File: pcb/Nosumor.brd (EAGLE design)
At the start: 50 x 50 mm, 122 parts, among them IC1 STM32F722RET, J3 SJ-43515TS-SMT-EDGE, K1 CHERRY-MX, K2 CHERRY-MX, K3 KSC623J, K4 KSC623J, K5 KSC623J, Q1 FDY100PZ, Q2 FDY100PZ, Q3 FDY100PZ, Q4 FDY100PZ, Q5 ABMM-6.000MHZ, Q6 CX2016DB, U2 AP2112K-3.3V, U3 USB3370, U4 TLV320AIC3110, U5 AP2112K-1.8V, U6 9DoF IMU

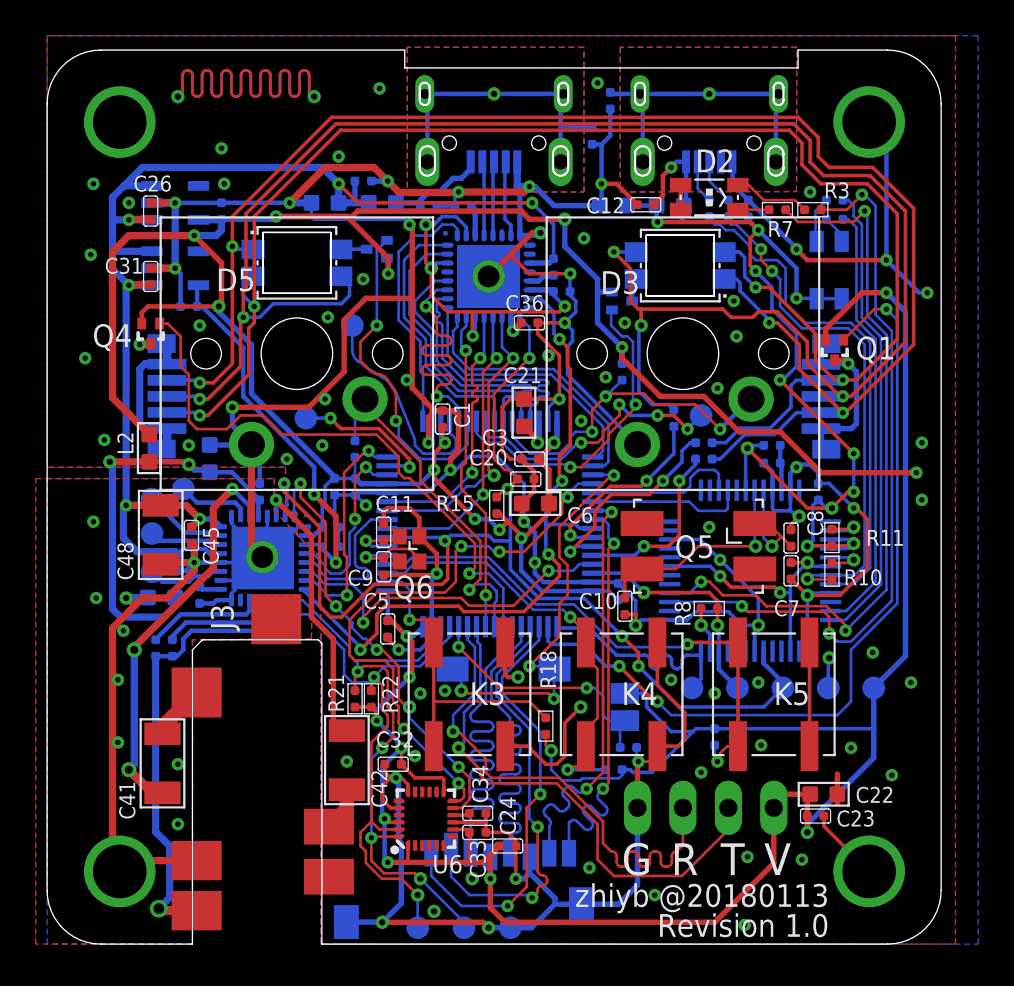
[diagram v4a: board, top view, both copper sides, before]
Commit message: PCB version 1.1 connected
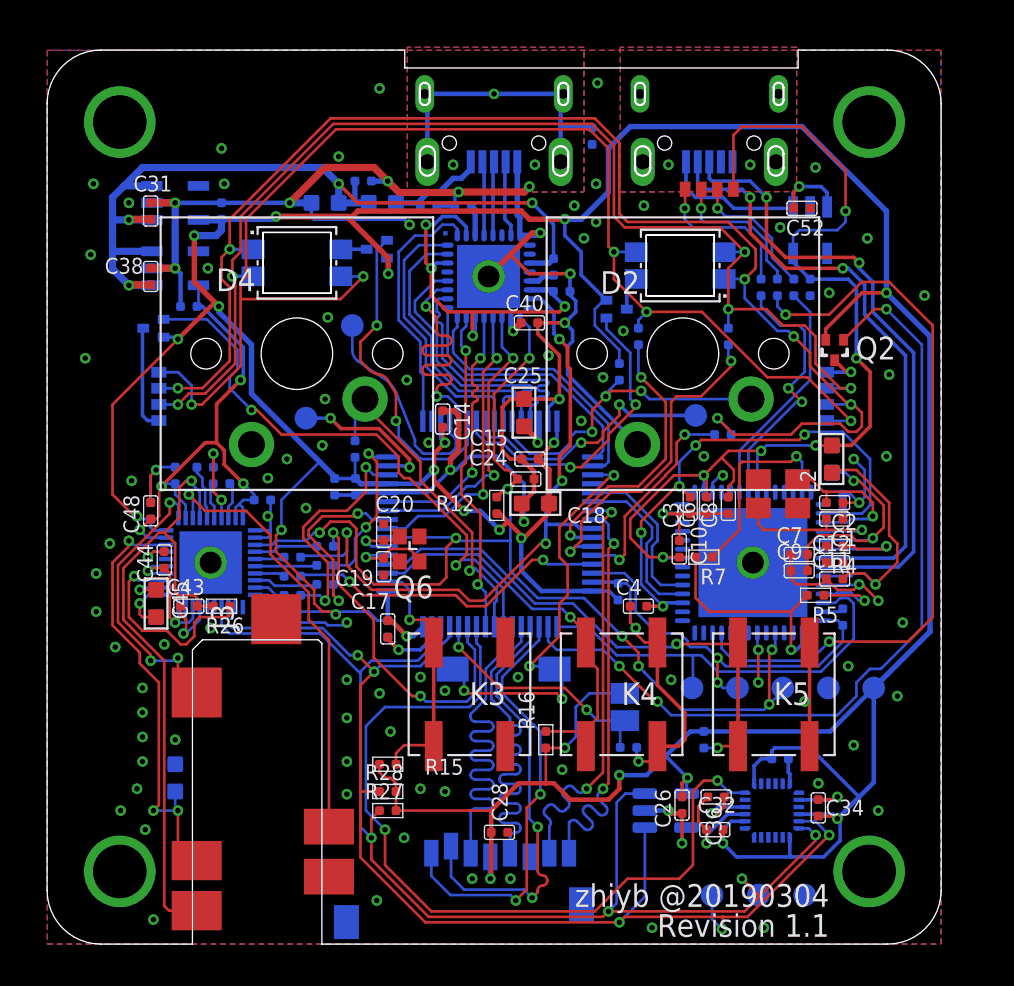
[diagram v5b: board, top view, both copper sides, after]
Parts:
- removed A2, GND$2, SCL, SDA, SLM, SLP, SRM, SRP: TPB1,27, testpad:B1,27
- removed D6: MSL0104RGBU1, led:2709
- removed JP1: (no value), pinhead:1X04
- added C50, C51: 100nf, Seeed-Capacitor:C0402
- added C52: 1UF 6.3V, Seeed-Capacitor:C0402
- added L4: 120OHM-500MA, Seeed-Inductor:L0603
- added R26: 2k7, Seeed-Resistor:R0402
- added R27, R28: 2k2, Seeed-Resistor:R0402
- added TP1, TP2, TP3, TP7: TPB1,27, testpad:B1,27
- added U7: AP2112K-1.8V, SparkFun-IC-Power:SOT23-5
- added U8: 24CW1280T-I/OT, 24CW1280T-I_OT:SOT95P280X145-5N
- C1, C2: value 100nf -> 4p
- C10, C8: value 18pf -> 100nf
- C11: value 12pf -> 4u7
- C13, C37, C39: value 100nf -> 1UF 6.3V
- C14, C33: value 10nf -> 100nf
- C17, C30, C35: value 1UF 6.3V -> 100nf
- C18: value 10uf -> 4.7uf
- C19, C20: value 100nf -> 12pf
- C21: value 4.7uf -> 10nf; device Seeed-Capacitor:C0603 -> Seeed-Capacitor:C0402
- C22: value 10uf -> 1UF 6.3V; device Seeed-Capacitor:C0603 -> Seeed-Capacitor:C0402
- C25: value 100nf -> 4.7uf; device Seeed-Capacitor:C0402 -> Seeed-Capacitor:C0603
- C26, C36: value 1UF 6.3V -> 100n
- C27, C32, C34: value 100nf -> 100n
- C28, C43, C44: value 10uf -> 100nf; device Seeed-Capacitor:C0603 -> Seeed-Capacitor:C0402
- C29, C46: value 100nf -> 2u2
- C4: value 100nf -> 3u3
- C40: value 470nf -> 1UF 6.3V
- C41: value 100uf -> 1UF 6.3V; device Seeed-Capacitor:C1206 -> Seeed-Capacitor:C0402
- C42, C48: value 100uf -> 100nf; device Seeed-Capacitor:C1206 -> Seeed-Capacitor:C0402
- C45, C47: value 100nf -> 10uf; device Seeed-Capacitor:C0402 -> Seeed-Capacitor:C0603
- C6: value 4.7uf -> 100nf; device Seeed-Capacitor:C0603 -> Seeed-Capacitor:C0402
- C7: value 33nf -> 4u7
- C9: value 12pf -> 100nf
- D1: value APBD3224SURKCGKC-F01 -> MSL0601RGB; device led:1210 -> led:1105
- D2: value APBD3224SURKCGKC-F01 -> HSMF-A3-BACK; device led:1210 -> led:HSMF-A3-BACK
- D3, D5: value HSMF-A3-BACK -> MSL0601RGB; device led:HSMF-A3-BACK -> led:1105
- D4: value MSL0104RGBU1 -> HSMF-A3-BACK; device led:2709 -> led:HSMF-A3-BACK
- Q1: value FDY100PZ -> ABM8W-12.0000MHZ; device transistor:SC-89 -> crystal:ABM8W
- Q5: value ABMM-6.000MHZ -> FDY100PZ; device crystal:ABMM -> transistor:SC-89
- R10: value 1.5K -> 150R
- R12, R13: value 22R -> 10K 1/16W
- R18, R19, R20: value 10K 1/16W -> 27R
- R2: value 150R -> 330R
- R21, R22: value 2.2K -> 27R
- R23: value 10K 1/16W -> 10R
- R24: value 20K -> 10K 1/16W
- R25: value 2.2K -> 20K
- R4: value 150R -> 12K 1/16W
- R5: value 330R -> 2k2
- R6: value 150R -> 470R 1/16W
- R7: value 330R -> 10K 1/16W
- R8, R9: value 470R 1/16W -> 150R
- U1: value (none) -> FT2232H-56Q-REEL; device ftdichip-6:LQFP48 -> FT2232H-56Q-REEL:QFN50P800X800X100-57N
- U3: value USB3370 -> AP2112K-3.3V; device microchip:QFN32 -> SparkFun-IC-Power:SOT23-5
- U4: value TLV320AIC3110 -> USB3370; device ti:VQFN32 -> microchip:QFN32
- U5: value AP2112K-1.8V -> TLV320AIC3256; device SparkFun-IC-Power:SOT23-5 -> ti:QFN40P500X500X80-41N
- moved C26 44.6 mm to (35.5, 7.77), turned to 180 degrees
- moved L2 38.2 mm to (43.9, 27.1)
- moved U2 35.5 mm to (42.7, 39.9), turned to 180 degrees
- moved Q5 32.8 mm to (5.94, 34.4), flipped to the bottom, turned to 270 degrees
- moved C42 32.4 mm to (17.7, 42.7), flipped to the bottom, turned to 90 degrees
- moved C22 32.3 mm to (16.1, 25.6), flipped to the bottom, turned to 180 degrees
- moved D4 30.2 mm to (14.0, 38.1), flipped to the top, turned to 270 degrees
- moved R25 30.1 mm to (28.3, 37.9), turned to 180 degrees
- moved C49 30.1 mm to (7.16, 26.2)
- moved C36 28.5 mm to (37.4, 8.23), turned to 90 degrees
- moved C27 27.8 mm to (41.0, 10.4)
- moved C40 27.7 mm to (27.0, 34.7), flipped to the top, turned to 270 degrees
- moved C5 26.4 mm to (44.5, 24.7), flipped to the bottom, turned to 0 degrees
- moved C23 26.1 mm to (19.1, 17.6), flipped to the bottom, turned to 180 degrees
- moved C41 25.6 mm to (7.92, 35.7), flipped to the bottom, turned to 270 degrees
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- renumbered A1 to TP4, BOOT to SJ1, CLK to TP6, D to TP8, DIO to TP9, GND to TP10, RST to TP5, VDD to TP11
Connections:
- removed net AVDD: C28.2, C29.2, C37.2, C43.2, L2.1, U4.17, U4.28
- removed net DBG_5V: C13.2, C16.2, C18.2, D1.1, D1.3, D2.1, D2.3, L1.1, R11.2, R9.2, U1.3, U1.4, U1.42
- removed net DBG_BM_U: J1.2, R12.2
- removed net DBG_DM: R12.1, U1.8
- removed net DBG_DP: R10.2, R13.1, U1.7
- removed net DBG_DP_U: J1.3, R13.2
- removed net DBG_SWD_LED1: R5.1, U1.12
- removed net DBG_SWD_LED2: R1.1, U1.11
- removed net N$10: C7.1, U1.14, U1.31, U1.6
- removed net N$27: C15.2, J1.Z1, J1.Z2, J1.Z3, J1.Z4
- removed net N$44: SRP.TP, U4.26
- removed net N$45: SRM.TP, U4.23
- removed net N$46: C40.1, U4.14
- removed net N$48: C42.1, U4.30
- removed net N$49: R25.1, U4.12
- removed net N$50: C41.1, U4.27
- removed net UART_RX: IC1.59, JP1.3
- removed net UART_TX: IC1.58, JP1.2
- new net DBG_1V8: C3.2, C4.2, C5.2, U1.2, U1.31, U1.43
- new net DBG_3V3: C10.2, C13.2, C6.2, C8.2, D1.CA, L1.2, L2.2, R5.2, R7.2, U1.16, U1.36, U1.44, U1.50, U2.5
- new net DBG_SWD_LED: R3.1, U1.25
- new net N$15: R7.1, U1.55
- new net N$16: D1.R, R1.2
- new net N$22: R20.2, U5.6
- new net N$40: R23.2, U5.5
- new net N$41: D1.B, R3.2
- new net N$42: C52.2, J1.1, U2.1, U2.3
- new net N$43: J1.3, U1.8
- new net N$51: J1.2, U1.7
- new net N$52: R4.1, U1.6
- new net N$53: R5.1, U1.11
- new net N$54: C7.2, C9.2, L1.1, U1.5
- new net N$55: C11.2, C12.2, L2.1, U1.9
- new net N$56: R6.2, U1.13
- new net N$8: C2.2, Q1.P$3, U1.3
- new net N$9: C1.2, Q1.P$1, U1.4
- net +1V8: now also C33.2, C41.2, C48.1, C49.1, U5.29, U5.32, U5.39, U5.40, U7.5; no longer C27.2, C38.2, U4.3, U5.5
- net +3V3: now also C15.2, C16.2, C18.2, C21.2, C26.2, C27.2, C28.1, C34.2, C35.2, C37.2, Q5.3, R12.2, R13.2, R14.2, R27.2, R28.2, U3.5, U5.10, U5.30, U8.4; no longer C1.2, C19.2, C24.1, C25.2, C3.2, C33.2, C4.2, C5.2, C6.2, JP1.1, L2.2, Q1.3, R18.2, R19.2, R20.2, R21.2, R22.2, U2.5, U4.2
- net +5V: now also C38.2, C42.2, C47.2, R25.2, U3.1, U3.3, U4.11, U7.1, U7.3; no longer C26.2, C39.2, C44.2, C45.2, C46.2, C48.2, R24.2, U2.1, U2.3, U3.11, U4.21, U4.24, U5.1, U5.3
- net ADC2: now also TP7.TP; no longer A2.TP
- net AIC_BCLK: now also R20.1; no longer U4.7
- net AIC_DIN: now also R19.1; no longer U4.5
- net AIC_DOUT: now also R21.1; no longer U4.4
- net AIC_GPIO: now also IC1.59, R18.1; no longer U4.32, U6.11
- net AIC_WCLK: now also R22.1; no longer U4.6
- net BOOT0: now also R11.1; no longer R14.1
- net DBG_RXD: now also U1.33; no longer U1.39
- net DBG_RX_LED: now also R2.1, U1.48; no longer R7.1, U1.28
- net DBG_TXD: now also U1.32; no longer U1.40
- net DBG_TX_LED: now also R1.1, U1.49; no longer R3.1, U1.27
- net GND: now also C2.1, C24.1, C28.2, C40.1, C41.1, C42.1, C44.2, C45.2, C48.2, C49.2, C50.1, C51.1, C52.1, C7.1, J1.Z1, J1.Z2, J1.Z3, J1.Z4, L4.2, R11.2, R24.1, R4.2, TP3.TP, U1.10, U1.21, U1.41, U1.57, U3.2, U4.8, U5.1, U5.11, U5.16, U5.21, U5.37, U5.41, U7.2, U8.2; no longer C2.2, C24.2, C28.1, C43.1, C44.1, C45.1, C46.1, C48.1, C49.1, C7.2, GND$2.TP, J3.4, JP1.4, R14.2, R23.1, U1.18, U1.25, U1.34, U1.47, U1.9, U3.8, U3.EXP, U4.1, U4.16, U4.18, U4.20, U4.25, U4.29
- net I2C_SCL: now also R28.1, TP2.TP, U5.13, U8.1; no longer R21.1, SCL.TP, U4.10
- net I2C_SDA: now also R27.1, TP1.TP, U5.14, U8.3; no longer R22.1, SDA.TP, U4.9
- net KEY_1: now also R13.1; no longer R16.1
- net KEY_2: now also R14.1; no longer R17.1
- net KEY_3: now also R15.1; no longer R18.1
- net KEY_4: now also R16.1; no longer R19.1
- net KEY_5: now also R17.1; no longer R20.1
- net LED_1: now also Q4.1; no longer Q3.1
- net LED_2: now also Q3.1; no longer Q2.1
- net LED_3: now also Q2.1; no longer Q1.1
- net LED_4: now also Q5.1; no longer Q4.1
- net LED_B: now also R8.1; no longer R2.1
- net LED_G: now also R10.1; no longer R6.1
- net LED_R: now also R9.1; no longer R4.1
- net MCLK: now also R23.1, U4.15; no longer U3.15, U4.8
- net MPU_INT: now also IC1.58; no longer IC1.36
- net N$1: now also R22.2, U5.7; no longer C41.2, J3.2
- net N$11: now also D3.CA, Q2.2; no longer C2.1, R9.1, U1.46
- net N$12: now also J3.3, U5.33; no longer D1.4, R5.2
- net N$13: now also J3.2, U5.31; no longer C12.2, J1.1, L1.2
- net N$14: now also J3.4, L4.1, U5.28; no longer R10.1, U1.5
- net N$17: now also C43.2, J3.1, R26.2, U5.34; no longer R11.1, U1.2
- net N$18: now also R26.1, U5.23; no longer C8.2, Q5.1, U1.44
- net N$19: now also C43.1, U5.17; no longer C10.2, Q5.3, U1.43
- net N$2: now also R19.2, U5.8; no longer C42.2, J3.3
- net N$20: now also C44.1, U5.18, U5.19, U5.20, U5.24, U5.25; no longer D2.4, R7.2
- net N$21: now also C45.1, U5.22; no longer D2.2, R3.2
- net N$23: now also C46.1, U5.36; no longer D1.2, R1.2
- net N$24: now also C19.2; no longer C9.2
- net N$25: now also C46.2, U5.38; no longer R8.2, U1.23
- net N$26: now also C20.2; no longer C11.2
- net N$28: now also D5.CA, Q5.2; no longer D6.1, D6.2, D6.6, D6.7, Q4.2
- net N$29: now also C25.2; no longer C21.2
- net N$3: now also R21.2, U5.9; no longer C40.2, J3.1, R25.2, U4.11
- net N$30: now also D1.G, R2.2; no longer SLM.TP, U4.19
- net N$31: now also C50.2; no longer C47.2
- net N$32: now also R25.1, U4.13; no longer R24.1, U3.13
- net N$33: now also C39.2, U4.14, U4.2, U4.22, U4.30; no longer C35.2, U3.14, U3.2, U3.22, U3.30
- net N$34: now also D4.2, Q4.2; no longer D5.2, Q3.2
- net N$35: now also C51.2; no longer C49.2
- net N$36: now also C40.2, U4.18; no longer C36.2, U3.18
- net N$37: now also R24.2, U4.3; no longer R23.2, U3.3
- net N$38: now also C29.2, U5.35; no longer D4.1, D4.2, D4.6, D4.7, Q1.2
- net N$39: now also D2.2, Q3.2; no longer D3.2, Q2.2
- net N$4: now also U4.4; no longer U3.4
- net N$47: now also C36.2; no longer C34.2
- net N$5: now also U4.5; no longer U3.5
- net N$6: now also U4.7; no longer U3.7
- net N$7: now also R18.2, U5.4; no longer SLP.TP, U4.22
- net NRST_N: now also U1.20; no longer U1.16
- net RGB_B: now also D2.1, D3.B, D4.1, D5.B, R8.2; no longer D3.1, D4.3, D5.1, D6.3, R2.2
- net RGB_G: now also D2.4, D3.G, D4.4, D5.G, R10.2; no longer D3.4, D4.5, D5.4, D6.5, R6.2
- net RGB_R: now also D2.3, D3.R, D4.3, D5.R, R9.2; no longer D3.3, D4.4, D5.3, D6.4, R4.2
- net SRST_N: now also C24.2, R12.1, U1.19, U4.17, U5.3; no longer C20.2, R15.1, U1.17, U3.17, U4.31
- net SWCLK: now also U1.12; no longer U1.24
- net SWDIO: now also R6.1, U1.14; no longer R8.1, U1.22
- net ULPI_CLK: now also U4.27; no longer U3.27
- net ULPI_D0: now also U4.1; no longer U3.1
- net ULPI_D1: now also U4.32; no longer U3.32
- net ULPI_D2: now also U4.31; no longer U3.31
- net ULPI_D3: now also U4.28; no longer U3.28
- net ULPI_D4: now also U4.26; no longer U3.26
- net ULPI_D5: now also U4.25; no longer U3.25
- net ULPI_D6: now also U4.24; no longer U3.24
- net ULPI_D7: now also U4.23; no longer U3.23
- net ULPI_DIR: now also U4.19; no longer U3.19
- net ULPI_NXT: now also U4.21; no longer U3.21
- net ULPI_STP: now also U4.20; no longer U3.20
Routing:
- net GND: track 399.8 -> 197.7 mm, vias 103 -> 121
- net DBG_3V3: track 0.00 -> 73.1 mm, vias 0 -> 7
- net DBG_5V: track 57.1 -> 0.00 mm, vias 11 -> 0
- net N$22: track 47.7 -> 3.47 mm, vias 2 -> 0
- net DBG_SWD_LED: track 0.00 -> 41.5 mm, vias 0 -> 2
- net N$43: track 0.00 -> 35.4 mm, vias 0 -> 2
- net I2C_SCL: track 33.3 -> 68.1 mm, vias 2 -> 5
- net N$17: track 2.64 -> 37.2 mm
- net N$51: track 0.00 -> 34.5 mm, vias 0 -> 2
- net I2C_SDA: track 34.4 -> 68.3 mm
- net DBG_1V8: track 0.00 -> 31.0 mm, vias 0 -> 5
- net DBG_DP: track 29.3 -> 0.00 mm, vias 3 -> 0
- net UART_TX: track 29.1 -> 0.00 mm, vias 1 -> 0
- net UART_RX: track 28.8 -> 0.00 mm, vias 1 -> 0
- net DBG_DM: track 28.6 -> 0.00 mm
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- removed copper zone on layer 1, net N$27
- removed copper zone on layer 16, net N$27
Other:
- board text added: "Revision 1.1"
- board text added: "zhiyb @20190304"
- board text removed: "R"
- board text removed: "Revision 1.0"
- board text removed: "T"
- board text removed: "V"
- board text removed: "zhiyb @20180113"

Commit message: PCB with silkscreen
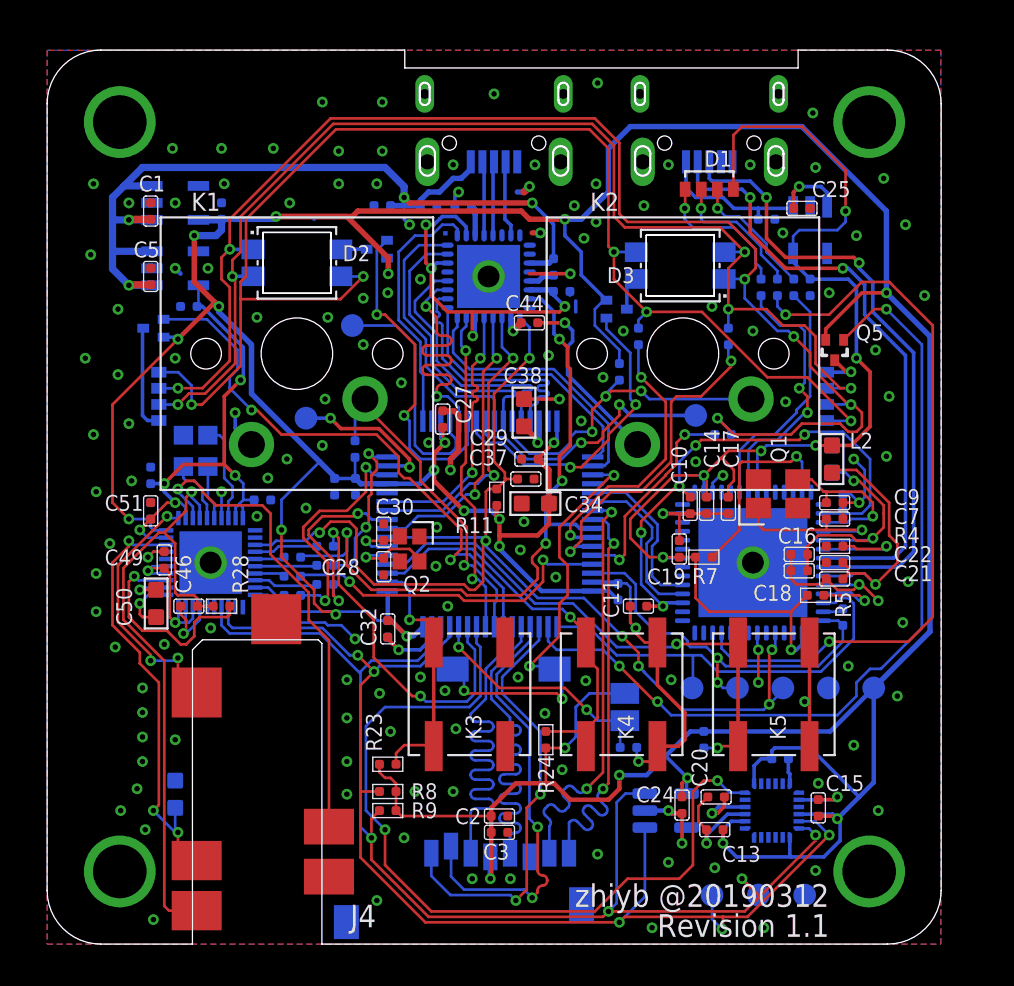
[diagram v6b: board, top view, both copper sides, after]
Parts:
- removed L4: 120OHM-500MA, Seeed-Inductor:L0603
- C1, C2: value 4p -> 4u7
- C13, C31, C37: value 1UF 6.3V -> 100n
- C15, C24, C33, C8: value 100nf -> 100n
- C16, C23, C35, C43, C44, C5, C6: value 100nf -> 4u7
- C18: value 4.7uf -> 100nf; device Seeed-Capacitor:C0603 -> Seeed-Capacitor:C0402
- C19: value 12pf -> 100nf
- C20: value 12pf -> 100n
- C21: value 10nf -> 4u7
- C22, C40, C41, C52: value 1UF 6.3V -> 100nf
- C25: value 4.7uf -> 4u7; device Seeed-Capacitor:C0603 -> Seeed-Capacitor:C0402
- C26: value 100n -> 100nf
- C28, C30: value 100nf -> 12pf
- C29: value 2u2 -> 100n
- C34: value 100n -> 4u7; device Seeed-Capacitor:C0402 -> Seeed-Capacitor:C0603
- C38: value 1UF 6.3V -> 4u7; device Seeed-Capacitor:C0402 -> Seeed-Capacitor:C0603
- C39: value 1UF 6.3V -> 2u2; device Seeed-Capacitor:C0402 -> rcl:C0603K
- C4: value 3u3 -> 4u7
- C45: value 10uf -> 4u7; device Seeed-Capacitor:C0603 -> Seeed-Capacitor:C0402
- C46: value 2u2 -> 100nf
- C47: value 10uf -> 2u2; device Seeed-Capacitor:C0603 -> rcl:C0603K
- C50: value 100nf -> 10uf; device Seeed-Capacitor:C0402 -> Seeed-Capacitor:C0603
- C7: value 4u7 -> 4p
- C9: value 100nf -> 4p
- D3: value MSL0601RGB -> HSMF-A3-BACK; device led:1105 -> led:HSMF-A3-BACK
- D4: value HSMF-A3-BACK -> MSL0601RGB; device led:HSMF-A3-BACK -> led:1105
- J3: value SJ-43515TS-SMT-EDGE -> (none); device connector:SJ-4351*-SMT-MIRRORED-EDGE -> Wurth_Elektronik_Electromechanic_Input-Output_Connectors_rev16b:629105150521
- J4: value (none) -> SJ-43515TS-SMT-EDGE; device Wurth_Elektronik_Electromechanic_Input-Output_Connectors_rev16b:629105150521 -> connector:SJ-4351*-SMT-MIRRORED-EDGE
- Q2: value FDY100PZ -> CX2016DB; device transistor:SC-89 -> crystal:CX2016DB
- Q6: value CX2016DB -> FDY100PZ; device crystal:CX2016DB -> transistor:SC-89
- R10: value 150R -> 10K 1/16W
- R12, R13, R14: value 10K 1/16W -> 100R
- R15, R16, R17: value 10K 1/16W -> 27R
- R20: value 27R -> 10R
- R21, R22: value 27R -> 10K 1/16W
- R23: value 10R -> 10K 1/16W
- R25: value 20K -> 10K 1/16W
- R26: value 2k7 -> 10K 1/16W
- R27: value 2k2 -> 20K
- R28: value 2k2 -> 2k7
- R4: value 12K 1/16W -> 12k 1%
- R6: value 470R 1/16W -> 330R
- R8, R9: value 150R -> 2k2
- U1: value FT2232H-56Q-REEL -> 3.3V; device FT2232H-56Q-REEL:QFN50P800X800X100-57N -> SparkFun-IC-Power:SOT23-5
- U2: value AP2112K-3.3V -> FT2232H-56Q-REEL; device SparkFun-IC-Power:SOT23-5 -> FT2232H-56Q-REEL:QFN50P800X800X100-57N
- U3: value AP2112K-3.3V -> 3.3V
- U4: value USB3370 -> 24CW1280T-I/OT; device microchip:QFN32 -> 24CW1280T-I_OT:SOT95P280X145-5N
- U5: value TLV320AIC3256 -> 9DoF IMU; device ti:QFN40P500X500X80-41N -> SparkFun-Sensors:QFN24-3X3
- U6: value 9DoF IMU -> 3.3V; device SparkFun-Sensors:QFN24-3X3 -> SparkFun-IC-Power:SOT23-5
- U7: value AP2112K-1.8V -> USB3370; device SparkFun-IC-Power:SOT23-5 -> microchip:QFN32
- U8: value 24CW1280T-I/OT -> TLV320AIC3256; device 24CW1280T-I_OT:SOT95P280X145-5N -> ti:QFN40P500X500X80-41N
- moved J3 48.1 mm to (25.0, 47.5), flipped to the bottom, turned to 180 degrees
- moved J4 48.1 mm to (12.1, 1.27), flipped to the top, turned to 90 degrees
- moved C1 42.0 mm to (5.79, 41.0), turned to 0 degrees
- moved C5 40.7 mm to (5.79, 37.3), flipped to the top
- moved C52 39.4 mm to (5.79, 26.2), flipped to the bottom, turned to 180 degrees
- moved Q5 38.1 mm to (44.0, 33.2), flipped to the top, turned to 180 degrees
- moved U1 38.1 mm to (7.16, 41.5), turned to 90 degrees
- moved TP2 37.7 mm to (17.1, 34.6), turned to 0 degrees
- moved TP8 35.5 mm to (46.2, 14.3)
- moved L3 35.0 mm to (7.16, 8.38), turned to 90 degrees
- moved U5 34.3 mm to (40.5, 7.47), turned to 90 degrees
- moved C31 33.7 mm to (31.9, 19.7), flipped to the bottom
- moved C26 33.1 mm to (40.2, 40.5), flipped to the bottom, turned to 90 degrees
- moved TP4 32.9 mm to (43.7, 14.3)
- moved U6 32.5 mm to (42.7, 39.9), turned to 180 degrees
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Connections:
- removed net N$31: C50.2, J4.1, L3.2
- removed net N$34 (its old number): D4.2, Q4.2
- removed net N$35: C51.2, J4.Z1, J4.Z2, J4.Z3, J4.Z4
- new net N$39: D3.2, Q4.2
- net +1V8: now also C51.1, C52.1, C6.2, U3.5, U8.29, U8.32, U8.39, U8.40; no longer C33.2, C48.1, C49.1, U5.29, U5.32, U5.39, U5.40, U7.5
- net +3V3: now also C13.2, C2.2, C24.2, C29.2, C3.1, C31.2, C33.2, C36.2, C4.2, C40.2, C42.2, C8.2, Q6.3, R11.2, R21.2, R22.2, R23.2, R24.2, R25.2, R8.2, R9.2, TP8.TP, U1.5, U4.4, U5.1, U5.13, U5.22, U5.8, U8.10, U8.30; no longer C14.2, C16.2, C17.2, C18.2, C21.2, C22.2, C23.2, C26.2, C28.1, C30.2, C37.2, Q2.3, R12.2, R13.2, R14.2, R15.2, R16.2, R17.2, R27.2, R28.2, TP11.TP, U3.5, U5.10, U5.30, U6.1, U6.13, U6.22, U6.8, U8.4
- net +5V: now also C1.2, C45.2, C48.2, C5.2, J3.1, R27.2, U1.1, U1.3, U7.11; no longer C31.2, C38.2, C42.2, C47.2, L3.1, R25.2, U4.11, U7.1, U7.3
- net ADC1: now also TP6.TP; no longer TP4.TP
- net ADC2: now also TP10.TP; no longer TP7.TP
- net AIC_BCLK: now also R17.1; no longer R20.1
- net AIC_DIN: now also R16.1; no longer R19.1
- net AIC_DOUT: now also R18.1; no longer R21.1
- net AIC_GPIO: now also R15.1; no longer R18.1
- net AIC_WCLK: now also R19.1; no longer R22.1
- net BOOT0: now also R10.1; no longer R11.1
- net DAC: now also TP2.TP; no longer TP8.TP
- net DBG_1V8: now also C10.2, C11.2, C12.2, U2.2, U2.31, U2.43; no longer C3.2, C4.2, C5.2, U1.2, U1.31, U1.43
- net DBG_3V3: now also C14.2, C17.2, C19.2, C23.2, U2.16, U2.36, U2.44, U2.50, U6.5; no longer C10.2, C13.2, C6.2, C8.2, U1.16, U1.36, U1.44, U1.50, U2.5
- net DBG_RXD: now also U2.33; no longer U1.33
- net DBG_RX_LED: now also U2.48; no longer U1.48
- net DBG_SWD_LED: now also U2.25; no longer U1.25
- net DBG_TXD: now also U2.32; no longer U1.32
- net DBG_TX_LED: now also U2.49; no longer U1.49
- net GND: now also C28.1, C3.2, C39.2, C43.1, C44.1, C45.1, C48.1, C50.2, C51.2, C52.2, J3.5, J3.Z1, J3.Z2, J3.Z3, J3.Z4, L3.2, Q2.2, R10.2, R26.1, TP4.TP, TP9.TP, U1.2, U2.10, U2.21, U2.41, U2.45, U2.57, U4.2, U5.18, U5.20, U5.9, U6.2, U7.8, U7.EXP, U8.1, U8.11, U8.16, U8.21, U8.37, U8.41; no longer C28.2, C3.1, C39.1, C44.2, C45.2, C47.1, C48.2, C50.1, C51.1, C52.1, J4.5, L4.2, Q6.2, R11.2, R24.1, TP10.TP, TP3.TP, U1.10, U1.21, U1.41, U1.45, U1.57, U2.2, U4.8, U4.EXP, U5.1, U5.11, U5.16, U5.2, U5.21, U5.37, U5.41, U6.18, U6.20, U6.9, U7.2
- net I2C_SCL: now also R8.1, TP5.TP, U4.1, U5.23, U8.13; no longer R28.1, TP2.TP, U5.13, U6.23, U8.1
- net I2C_SDA: now also R9.1, U4.3, U5.24, U8.14; no longer R27.1, U5.14, U6.24, U8.3
- net KEY_1: now also R21.1; no longer R13.1
- net KEY_2: now also R22.1; no longer R14.1
- net KEY_3: now also R23.1; no longer R15.1
- net KEY_4: now also R24.1; no longer R16.1
- net KEY_5: now also R25.1; no longer R17.1
- net LED_1: now also Q3.1; no longer Q4.1
- net LED_2: now also Q4.1; no longer Q3.1
- net LED_3: now also Q5.1; no longer Q2.1
- net LED_4: now also Q6.1; no longer Q5.1
- net LED_B: now also R14.1; no longer R8.1
- net LED_G: now also R13.1; no longer R10.1
- net LED_R: now also R12.1; no longer R9.1
- net MCLK: now also R20.1, U7.15; no longer R23.1, U4.15
- net MPU_INT: now also U5.12; no longer U6.12
- net N$1: now also R19.2, U8.7; no longer R22.2, U5.7
- net N$11: now also D4.CA, Q5.2; no longer D3.CA, Q2.2
- net N$12: now also J4.3, U8.33; no longer J3.3, U5.33
- net N$13: now also J4.2, U8.31; no longer J3.2, U5.31
- net N$14: now also J4.4, L3.1, U8.28; no longer J3.4, L4.1, U5.28
- net N$15: now also U2.55; no longer U1.55
- net N$17: now also C46.2, J4.1, R28.2, U8.34; no longer C43.2, J3.1, R26.2, U5.34
- net N$18: now also R28.1, U8.23; no longer R26.1, U5.23
- net N$19: now also C46.1, U8.17; no longer C43.1, U5.17
- net N$2: now also R16.2, U8.8; no longer R19.2, U5.8
- net N$20: now also C49.1, U8.18, U8.19, U8.20, U8.24, U8.25; no longer C44.1, U5.18, U5.19, U5.20, U5.24, U5.25
- net N$21: now also C50.1, U8.22; no longer C45.1, U5.22
- net N$22: now also R17.2, U8.6; no longer R20.2, U5.6
- net N$23: now also C47.1, U8.36; no longer C46.1, U5.36
- net N$24: now also C28.2, Q2.1; no longer C19.2, Q6.1
- net N$25: now also C47.2, U8.38; no longer C46.2, U5.38
- net N$26: now also C30.2, Q2.3; no longer C20.2, Q6.3
- net N$28: now also Q6.2; no longer Q5.2
- net N$29: now also C38.2; no longer C25.2
- net N$3: now also R18.2, U8.9; no longer R21.2, U5.9
- net N$32: now also R27.1, U7.13; no longer R25.1, U4.13
- net N$33: now also C43.2, U7.14, U7.2, U7.22, U7.30; no longer C39.2, U4.14, U4.2, U4.22, U4.30
- net N$36: now also C44.2, U7.18; no longer C40.2, U4.18
- net N$37: now also R26.2, U7.3; no longer R24.2, U4.3
- net N$38: now also C39.1, U8.35; no longer C29.2, U5.35
- net N$4: now also J3.2, U7.4; no longer J4.2, U4.4
- net N$40: now also R20.2, U8.5; no longer R23.2, U5.5
- net N$42: now also C25.2, C26.2, U6.1, U6.3; no longer C52.2, U2.1, U2.3
- net N$43: now also U2.8; no longer U1.8
- net N$47: now also C20.2, U5.10; no longer C36.2, U6.10
- net N$5: now also J3.3, U7.5; no longer J4.3, U4.5
- net N$51: now also U2.7; no longer U1.7
- net N$52: now also U2.6; no longer U1.6
- net N$53: now also U2.11; no longer U1.11
- net N$54: now also C16.2, C18.2, U2.5; no longer C7.2, C9.2, U1.5
- net N$55: now also C21.2, C22.2, U2.9; no longer C11.2, C12.2, U1.9
- net N$56: now also U2.13; no longer U1.13
- net N$6: now also J3.4, U7.7; no longer J4.4, U4.7
- net N$7: now also R15.2, U8.4; no longer R18.2, U5.4
- net N$8: now also C9.2, U2.3; no longer C2.2, U1.3
- net N$9: now also C7.2, U2.4; no longer C1.2, U1.4
- net NRST_N: now also U2.20; no longer U1.20
- net RGB_B: now also D3.1, D4.B, R14.2; no longer D3.B, D4.1, R8.2
- net RGB_G: now also D3.4, D4.G, R13.2; no longer D3.G, D4.4, R10.2
- net RGB_R: now also D3.3, D4.R, R12.2; no longer D3.R, D4.3, R9.2
- net SRST_N: now also C37.2, R11.1, TP11.TP, U2.19, U7.17, U8.3; no longer C24.2, R12.1, TP5.TP, U1.19, U4.17, U5.3
- net SWCLK: now also TP3.TP, U2.12; no longer TP6.TP, U1.12
- net SWDIO: now also TP7.TP, U2.14; no longer TP9.TP, U1.14
- net ULPI_CLK: now also U7.27; no longer U4.27
- net ULPI_D0: now also U7.1; no longer U4.1
- net ULPI_D1: now also U7.32; no longer U4.32
- net ULPI_D2: now also U7.31; no longer U4.31
- net ULPI_D3: now also U7.28; no longer U4.28
- net ULPI_D4: now also U7.26; no longer U4.26
- net ULPI_D5: now also U7.25; no longer U4.25
- net ULPI_D6: now also U7.24; no longer U4.24
- net ULPI_D7: now also U7.23; no longer U4.23
- net ULPI_DIR: now also U7.19; no longer U4.19
- net ULPI_NXT: now also U7.21; no longer U4.21
- net ULPI_STP: now also U7.20; no longer U4.20
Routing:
- net GND: track 197.7 -> 105.9 mm, vias 121 -> 159
- net N$35: track 17.3 -> 0.00 mm, vias 3 -> 0
- net N$31: track 5.67 -> 0.00 mm
- net N$25: track 2.09 -> 5.68 mm
- net N$12: track 24.6 -> 27.1 mm
- net N$39: track 0.00 -> 2.02 mm
- net DAC: track 12.2 -> 13.8 mm
- net N$34 (its old number): track 1.46 -> 0.00 mm
- net N$17: track 37.2 -> 35.8 mm
- net N$13: track 16.0 -> 14.6 mm
- net SRST_N: track 64.1 -> 65.3 mm, vias 8 -> 7
- net +3V3: track 278.9 -> 280.1 mm
- net +5V: track 50.7 -> 51.8 mm
- net +1V8: track 29.3 -> 28.3 mm, vias 4 -> 5
- net N$23: track 2.08 -> 3.03 mm
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- removed copper zone on layer 1, net N$35
- removed copper zone on layer 16, net N$35
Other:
- board text added: ">w<"
- board text added: "R"
- board text added: "V"
- board text added: "zhiyb @20190312"
- board text removed: "zhiyb @20190304"

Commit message: PCB revision 1.2, fix RGB LED footprint
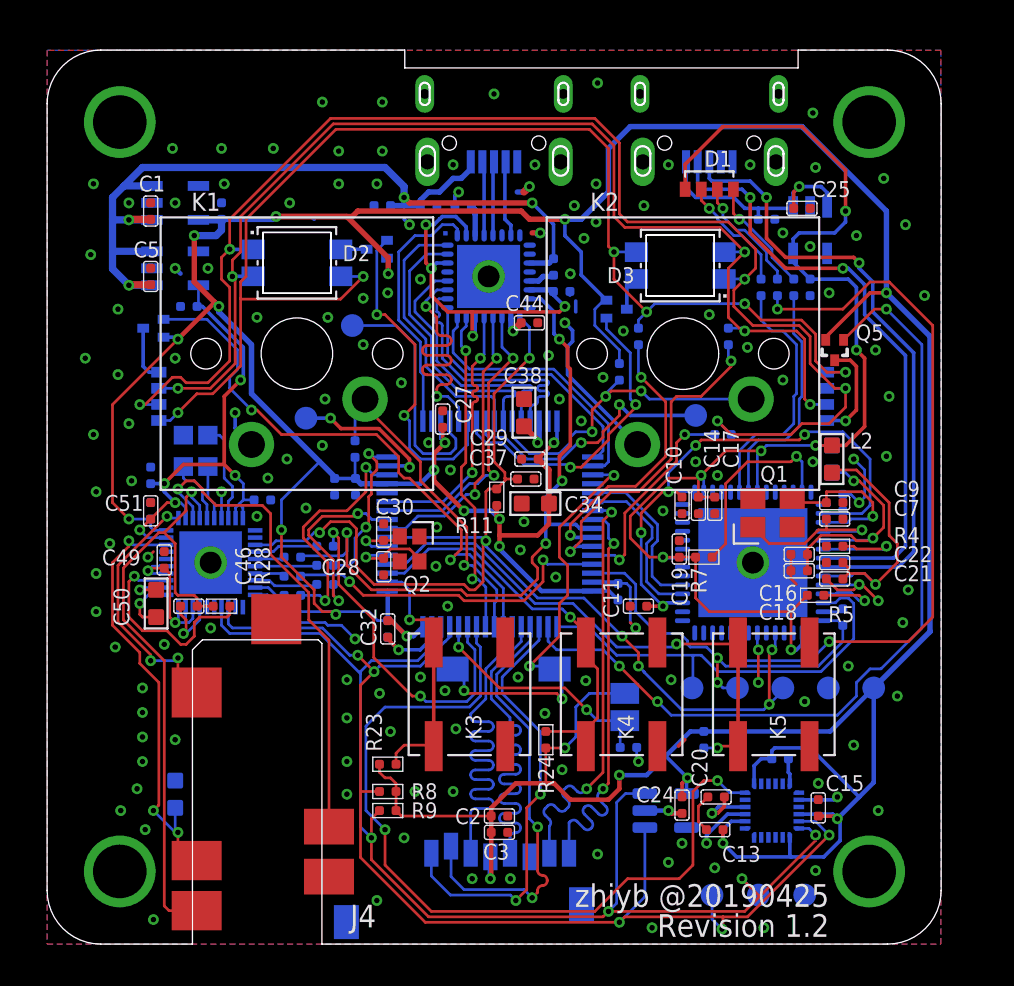
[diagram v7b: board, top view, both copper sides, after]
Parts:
- moved R1 1.83 mm to (41.8, 36.7)
- moved R2 1.83 mm to (39.9, 36.7)
- moved Q1 1.11 mm to (39.5, 23.3)
- moved C17 0.76 mm to (37.3, 24.5)
- moved C10 0.46 mm to (35.5, 24.5)
- moved C14 0.46 mm to (36.4, 24.5)
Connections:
- net DBG_SWD_LED: now also U2.24; no longer U2.25
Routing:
- net GND: track 105.9 -> 64.3 mm, vias 159 -> 161
- net N$11: track 2.56 -> 5.74 mm
- net N$28: track 5.92 -> 3.14 mm
- net RGB_B: track 77.5 -> 79.3 mm, vias 6 -> 5
- net DBG_TX_LED: track 15.0 -> 13.3 mm, vias 2 -> 0
- net N$16: track 8.14 -> 6.51 mm
- net RGB_G: track 67.2 -> 65.8 mm
- net RGB_R: track 74.4 -> 72.9 mm, vias 5 -> 6
- net N$41: track 7.87 -> 6.68 mm
- net DBG_RX_LED: track 13.6 -> 14.4 mm
- net DBG_SWD_LED: track 41.5 -> 40.9 mm
- net DBG_1V8: track 31.0 -> 31.6 mm
- net N$30: track 7.24 -> 6.68 mm
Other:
- board text added: "Revision 1.2"
- board text added: "zhiyb @20190425"
- board text removed: "Revision 1.1"
- board text removed: "zhiyb @20190312"
